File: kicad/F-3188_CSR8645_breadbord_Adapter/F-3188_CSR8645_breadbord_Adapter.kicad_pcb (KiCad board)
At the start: 2 copper layers, 23.9 x 56.9 mm, 4 parts, among them J1 SCJ368R1NUS0B00G, P1 CONN_01X22, P2 CONN_01X21, U1 F-3188_CSR8645

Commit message: to fcking much changes to commit it separatly, lets go with everything in one commit, git will love me for sure :D
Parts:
- added D1: LED1, LEDs:LED_1206, F.Cu at (113.3, 79.8)
- added D2: LED1, LEDs:LED_1206, F.Cu at (113.3, 85.2)
- added R1: 10k, Resistors_SMD:R_0805, F.Cu at (117.9, 79.9)
- added R2: 10k, Resistors_SMD:R_0805, F.Cu at (121.5, 79.9)
- added R3: 1k, Resistors_SMD:R_0805, F.Cu at (117.9, 85.3)
- added R4: 1k, Resistors_SMD:R_0805, F.Cu at (121.5, 85.3)
- added SW1: RESET, Buttons_Switches_SMD:SW_SPST_FSMSM, F.Cu at (104.2, 80.8)
- added SW2: POWER_ON, Buttons_Switches_SMD:SW_SPST_FSMSM, F.Cu at (104.2, 88.5)
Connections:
- net Net-(J1-Pad1) renamed /HGND
- net Net-(P1-Pad13) renamed /RST#
- net Net-(P1-Pad14) renamed /BAT
- net Net-(P1-Pad15) renamed /POWER_ON
- net Net-(P1-Pad2) renamed /LED1
- net Net-(P1-Pad3) renamed /LED0
- J1 pad 2: Net-(J1-Pad2) -> /HL
- J1 pad 3: (no net) -> /HL
- J1 pad 4: (no net) -> /HR
- J1 pad 5: Net-(J1-Pad5) -> /HR
- P2 pad 2: Net-(J1-Pad5) -> /HR
- P2 pad 4: Net-(J1-Pad2) -> /HL
- U1 pad 40: Net-(J1-Pad2) -> /HL
- U1 pad 42: Net-(J1-Pad5) -> /HR
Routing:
- net /HL: track 0.00 -> 65.8 mm, vias 0 -> 1
- net /HR: track 0.00 -> 63.9 mm, vias 0 -> 1
- net Net-(J1-Pad2): track 63.1 -> 0.00 mm, vias 1 -> 0
- net Net-(J1-Pad5): track 61.5 -> 0.00 mm, vias 1 -> 0

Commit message: new version
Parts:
- removed SW1: RESET, Buttons_Switches_SMD:SW_SPST_FSMSM
- added J2: ON, Jumper:SolderJumper-2_P1.3mm_Open_RoundedPad1.0x1.5mm, B.Cu at (145.0, 82.8)
- added RESET: RESET, Buttons_Switches_SMD:SW_SPST_FSMSM, B.Cu at (145.0, 105.4)
- D1, D2, R1, R2, R3, R4: moved to B.Cu
- POWER ON: renamed from SW2; moved to B.Cu
- moved POWER ON 40.9 mm to (145.0, 90.8), turned to 270 degrees
- moved D1 34.9 mm to (146.8, 70.2), turned to 270 degrees
- moved D2 33.0 mm to (142.7, 70.2), turned to 270 degrees
- moved R1 30.2 mm to (140.8, 99.6), turned to 270 degrees
- moved R3 28.0 mm to (144.7, 77.2)
- moved R4 25.5 mm to (144.7, 74.7)
- moved R2 23.2 mm to (144.7, 79.8)
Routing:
- net /GND: track 56.2 -> 109.9 mm, vias 3 -> 9
- net /BAT: track 26.3 -> 50.5 mm
- net /POWER_ON: track 28.9 -> 44.3 mm
- net /HGND: track 78.1 -> 62.9 mm, vias 2 -> 1
- net /RST#: track 24.2 -> 34.5 mm
- net /LED1: track 5.44 -> 15.8 mm, vias 0 -> 1
- net Net-(P1-Pad16): track 31.7 -> 41.7 mm
- net Net-(J2-Pad2): track 0.00 -> 8.58 mm
- net /HL: track 65.8 -> 59.0 mm
- net Net-(D1-Pad2): track 0.00 -> 5.81 mm
- net Net-(D2-Pad2): track 0.00 -> 4.59 mm
- net Net-(P2-Pad16): track 30.8 -> 27.5 mm
- net /LED0: track 9.13 -> 12.2 mm
- net Net-(P1-Pad19): track 30.1 -> 32.3 mm
- net /HR: track 63.9 -> 61.7 mm
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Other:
- board size 23.9 x 56.9 mm -> 24.4 x 57.4 mm
- board text added: "+"
- board text added: "-"
- board text added: "13"
- board text added: "BAT SEN"
- board text added: "CHG EXT"
- board text added: "POWER ON"
- board text added: "RST"
- board text added: "USB"
- board text removed: "BAT SENSE"
- board text removed: "CHG_EXT"
- board text removed: "PIO"
- board text removed: "PIO13"
- board text removed: "POWER_RN"
- board text removed: "RST#"
- board text removed: "USB _P _N"

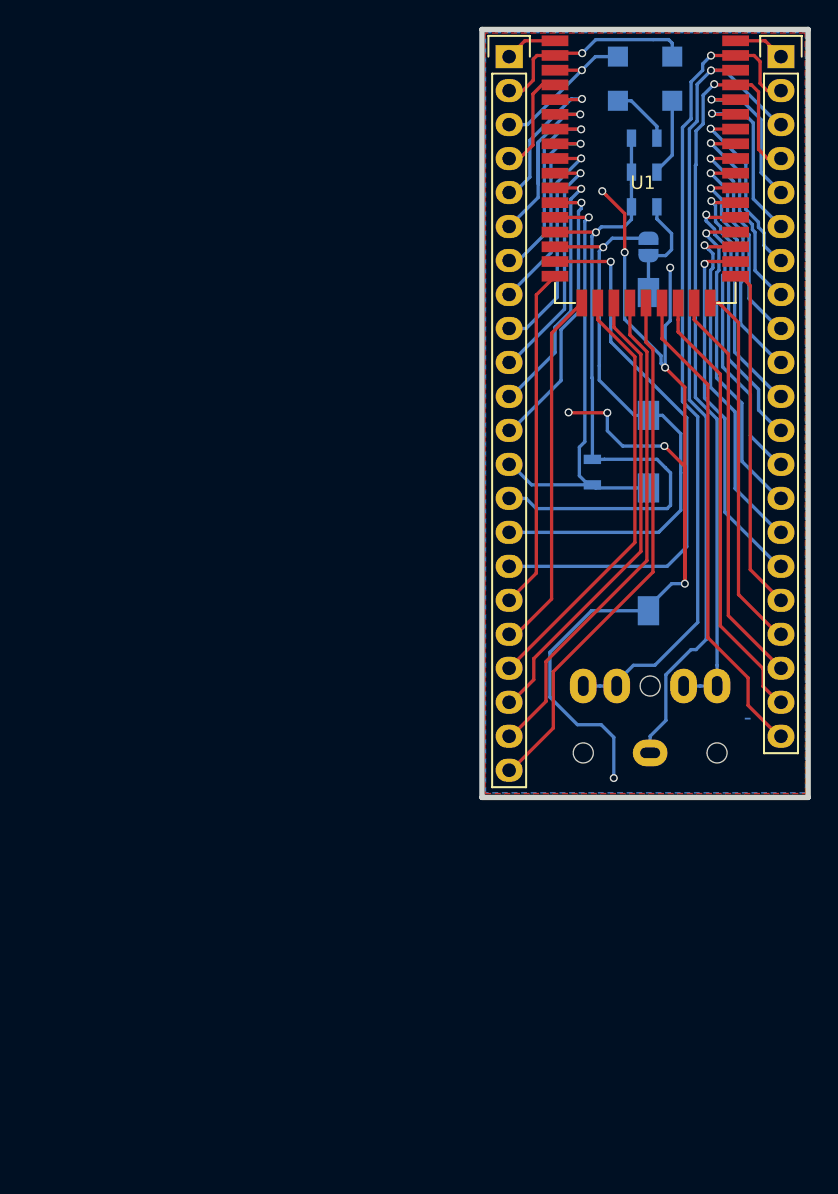
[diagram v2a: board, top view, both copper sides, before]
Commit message: v2, buttons, mic support, 3leds usb port
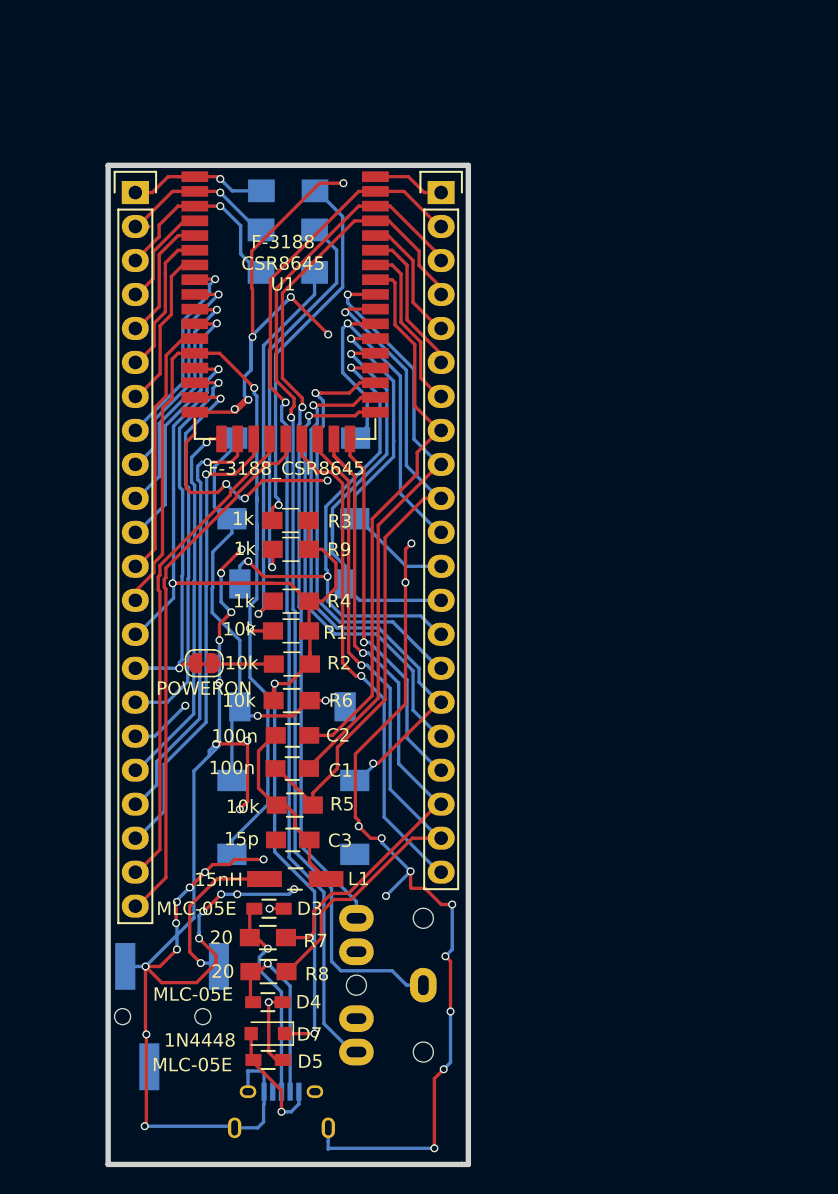
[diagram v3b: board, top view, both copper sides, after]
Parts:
- removed POWER ON: POWER_ON, Buttons_Switches_SMD:SW_SPST_FSMSM
- removed RESET: RESET, Buttons_Switches_SMD:SW_SPST_FSMSM
- added C1: 100n, Capacitors_SMD.pretty:C_0805_HandSoldering, F.Cu at (118.4, 121.8)
- added C2: 100n, Capacitors_SMD.pretty:C_0805_HandSoldering, F.Cu at (118.4, 119.3)
- added C3: 15p, Capacitors_SMD.pretty:C_0805_HandSoldering, F.Cu at (118.4, 127.1)
- added D3: MLC-05E, Resistors_SMD.pretty:R_0603_HandSoldering, F.Cu at (116.7, 132.3)
- added D4: MLC-05E, Resistors_SMD.pretty:R_0603_HandSoldering, F.Cu at (116.6, 139.3)
- added D5: MLC-05E, Resistors_SMD.pretty:R_0603_HandSoldering, F.Cu at (116.6, 143.6)
- added D6: LED1, LEDs:LED_1206_HandSoldering, B.Cu at (118.1, 78.6)
- added D7: 1N4448, Diodes_SMD:D_SOD-323_HandSoldering, F.Cu at (116.6, 141.6)
- added JP1: POWERON, Jumper:SolderJumper-2_P1.3mm_Open_RoundedPad1.0x1.5mm, F.Cu at (111.8, 113.9)
- added L1: 15nH, Choke_SMD.pretty:Choke_SMD_1206_Handsoldering, F.Cu at (118.6, 130.0)
- added R5: 10k, Resistors_SMD.pretty:R_0805_HandSoldering, F.Cu at (118.6, 124.5)
- added R6: 10k, Resistors_SMD.pretty:R_0805_HandSoldering, F.Cu at (118.4, 116.7)
- added R7: 20, Resistors_SMD.pretty:R_0805_HandSoldering, F.Cu at (116.6, 134.4)
- added R8: 20, Resistors_SMD.pretty:R_0805_HandSoldering, F.Cu at (116.6, 137.0)
- added R9: 1k, Resistors_SMD:R_0805_HandSoldering, F.Cu at (118.3, 105.4)
- added SW1: RESET, Buttons_Switches_SMD:SW_SPST_FSMSM, B.Cu at (118.5, 128.2)
- added SW2: VOL+, Buttons_Switches_SMD:SW_SPST_FSMSM, B.Cu at (118.6, 97.1)
- added SW3: VOL-, Buttons_Switches_SMD:SW_SPST_FSMSM, B.Cu at (118.5, 103.1)
- added SW4: NEXt, Buttons_Switches_SMD:SW_SPST_FSMSM, B.Cu at (122.4, 112.6)
- added SW5: PREV, Buttons_Switches_SMD:SW_SPST_FSMSM, B.Cu at (114.5, 112.6)
- added SW6: PLAY, Buttons_Switches_SMD:SW_SPST_FSMSM, B.Cu at (118.5, 122.7)
- added U2: MIC, jacks:3.5mm_stereo_jack_PJ320B, B.Cu at (105.7, 140.3)
- D1, D2: footprint LEDs:LED_1206 -> LEDs:LED_1206_HandSoldering
- J1: footprint jacks:3.5mm_stereo_jack_PJ306M_no_screw_terminal -> jacks:3.5mm_stereo_jack_PJ306M
- J2: value ON -> USB_B_Micro; footprint Jumper:SolderJumper-2_P1.3mm_Open_RoundedPad1.0x1.5mm -> Connect.pretty:USB_Micro-B
- R1, R2, R3, R4: footprint Resistors_SMD:R_0805 -> Resistors_SMD:R_0805_HandSoldering; moved to F.Cu
- moved J2 70.3 mm to (117.6, 147.5), turned to 180 degrees
- moved R4 43.5 mm to (118.3, 109.3), turned to 180 degrees
- moved R2 43.1 mm to (118.4, 114.0), turned to 180 degrees
- moved R3 37.1 mm to (118.3, 103.3), turned to 180 degrees
- moved D1 30.9 mm to (118.1, 81.5), turned to 0 degrees
- moved P1 29.7 mm to (106.7, 78.7)
- moved U1 28.8 mm to (111.1, 97.2)
- moved D2 28.6 mm to (118.1, 84.7), turned to 0 degrees
- moved P2 27.4 mm to (129.5, 78.7)
- moved R1 25.5 mm to (118.3, 111.5), turned to 180 degrees
- moved J1 24.3 mm to (128.2, 138.0), turned to 90 degrees
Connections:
- net Net-(P1-Pad1) renamed /LED2
- net Net-(P2-Pad10) renamed /MIC_BIAS
- net Net-(P2-Pad11) renamed /VOLUP
- net Net-(P2-Pad12) renamed /VOLDOWN
- net Net-(P2-Pad13) renamed /NEXT
- net Net-(P2-Pad14) renamed /PREV
- net Net-(P2-Pad16) renamed /PLAY
- net Net-(P2-Pad18) renamed /MUTE
- net Net-(P2-Pad19) renamed /USB+
- net Net-(P2-Pad20) renamed /USB-
- net Net-(P2-Pad6) renamed /MIC_BP
- net Net-(P2-Pad7) renamed /MIC_BN
- net Net-(P2-Pad8) renamed /MIC_AP
- net Net-(P2-Pad9) renamed /MIC_AN
- J1 pad 3: /HL -> (no net)
- J1 pad 4: /HR -> (no net)
- J2 pad 1: /POWER_ON -> 5V
- J2 pad 2: Net-(J2-Pad2) -> Net-(D4-Pad1)
- P1 pad 17: /GND -> GND
- R2 pad 2: Net-(J2-Pad2) -> /POWER_ON
- R3 pad 2: Net-(D1-Pad2) -> Net-(D6-Pad2)
- U1 pad 17: /GND -> GND
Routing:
- net GND: track 0.00 -> 236.7 mm, vias 0 -> 45
- net /GND: track 109.9 -> 0.00 mm, vias 9 -> 0
- net /BAT: track 50.5 -> 92.3 mm, vias 1 -> 4
- net Net-(R6-Pad1): track 0.00 -> 37.5 mm, vias 0 -> 2
- net /RST#: track 34.5 -> 67.5 mm, vias 1 -> 2
- net /MIC_BIAS: track 18.4 -> 51.2 mm
- net Net-(D6-Pad2): track 0.00 -> 28.1 mm, vias 0 -> 1
- net /MIC_AN: track 16.8 -> 44.7 mm
- net /MIC_AP: track 15.5 -> 41.9 mm, vias 1 -> 0
- net Net-(D2-Pad2): track 4.59 -> 28.7 mm, vias 0 -> 1
- net Net-(D1-Pad2): track 5.81 -> 29.5 mm, vias 0 -> 1
- net /USB+: track 30.0 -> 49.3 mm, vias 0 -> 1
- net /USB-: track 33.1 -> 50.8 mm, vias 0 -> 1
- net /HR: track 61.7 -> 77.4 mm
- net Net-(D3-Pad1): track 0.00 -> 15.7 mm, vias 0 -> 1
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- added copper zone on B.Cu, net GND
- added copper zone on F.Cu, net GND
- removed copper zone on B.Cu, net /GND
- removed copper zone on F.Cu, net /GND
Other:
- board size 24.4 x 57.4 mm -> 26.9 x 74.7 mm
- board text added: "F-3188 CSR8645"
- board text added: "NEXT"
- board text added: "PLAY"
- board text added: "PR EV"
- board text added: "VOL+"
- board text added: "VOL-"
- board text removed: "18"
- board text removed: "19"
- board text removed: "20"
- board text removed: "21"
- board text removed: "7"
- board text removed: "BIAS"
